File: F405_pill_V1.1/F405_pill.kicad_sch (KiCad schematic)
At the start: 50 parts, among them J1 Conn_01x04_Male, J2 Conn_01x04_Male, J4 TYPE-C-31-M-12, U1 STM32F405RGTx, U2 MAX3051EKA+T, U3 LM1117-3.3, U4 STM32F405_pill, U5 HT7550-1, Y1 Crystal_GND24

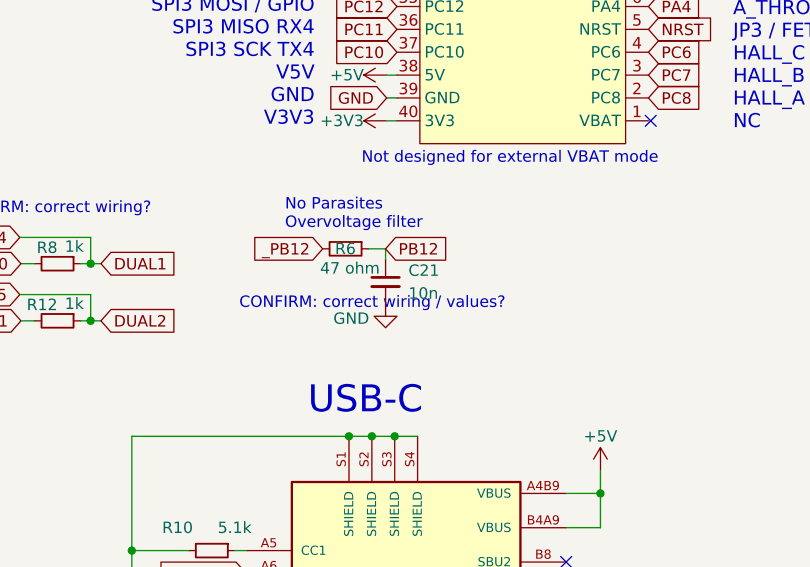
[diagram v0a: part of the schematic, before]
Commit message: changed some part numbers to jlcpcb basic parts
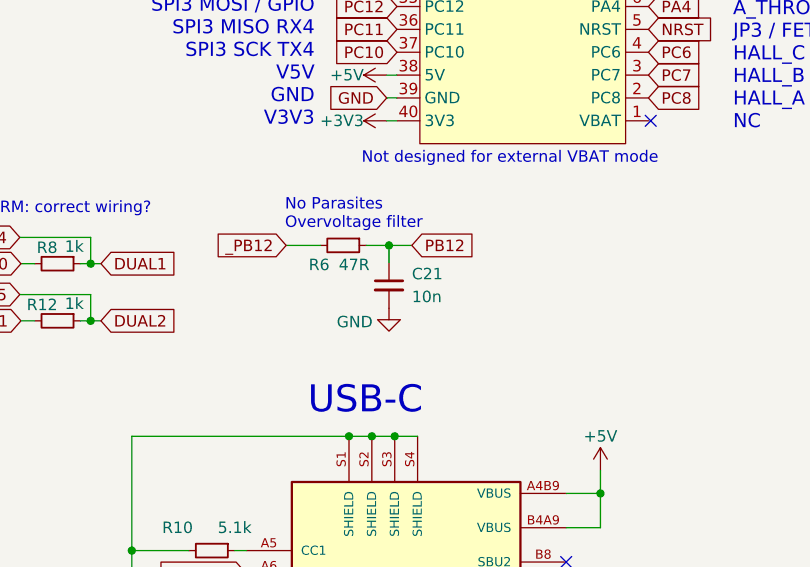
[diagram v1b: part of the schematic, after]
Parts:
- C14, C15: LCSC C41851 -> C1546
- C21, C8: LCSC C527024 -> C15195
- R12, R8: LCSC C25543 -> C11702
- R6: value 47 ohm -> 47R
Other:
- note removed: "CONFIRM: correct wiring / values?"
- moved on the sheet: C21
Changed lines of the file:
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@@
   (junction (at 88.265 115.062) (diameter 0) (color 0 0 0 0)
   )
+  (junction (at 170.815 93.98) (diameter 0) (color 0 0 0 0)
+  )
   (junction (at 69.215 162.052) (diameter 0) (color 0 0 0 0)
   )
@@
     (stroke (width 0) (type default) (color 0 0 0 0))
   )
+  (wire (pts (xy 159.385 93.98) (xy 163.195 93.98))
+    (stroke (width 0) (type default) (color 0 0 0 0))
+  )
   (wire (pts (xy 225.044 135.89) (xy 225.044 134.62))
     (stroke (width 0) (type default) (color 0 0 0 0))
@@
     (stroke (width 0) (type default) (color 0 0 0 0))
   )
+  (wire (pts (xy 170.815 93.98) (xy 168.275 93.98))
+    (stroke (width 0) (type default) (color 0 0 0 0))
+  )
   (wire (pts (xy 146.431 165.862) (xy 144.272 165.862))
     (stroke (width 0) (type default) (color 0 0 0 0))
@@
     (stroke (width 0) (type default) (color 0 0 0 0))
   )
+  (wire (pts (xy 170.815 93.98) (xy 170.815 95.885))
+    (stroke (width 0) (type default) (color 0 0 0 0))
+  )
   (wire (pts (xy 28.702 103.759) (xy 28.702 105.664))
     (stroke (width 0) (type default) (color 0 0 0 0))
@@
     (stroke (width 0) (type default) (color 0 0 0 0))
   )
-  (wire (pts (xy 170.434 95.504) (xy 170.434 94.361))
-    (stroke (width 0) (type default) (color 0 0 0 0))
-  )
   (wire (pts (xy 146.431 171.831) (xy 146.431 173.482))
     (stroke (width 0) (type default) (color 0 0 0 0))
@@
     (stroke (width 0) (type default) (color 0 0 0 0))
   )
-  (wire (pts (xy 170.434 94.361) (xy 168.529 94.361))
+  (wire (pts (xy 173.355 93.98) (xy 170.815 93.98))
     (stroke (width 0) (type default) (color 0 0 0 0))
   )
@@
     (effects (font (size 1.27 1.27)) (justify left bottom))
   )
-  (text "CONFIRM: correct wiring / values?" (at 154.178 101.219 0)
-    (effects (font (size 1.27 1.27)) (justify left bottom))
-  )
   (text "Changes: \nXtal caps from 18pF to 12pF\nSeparate the two LEDs from the single resistor\nNew CAN, with spike protection\nRC between GND and pb12 to stop false trips\nPC12->PA15 to drive LED\nIncreased functionality of several header pins\n"
     (at 155.067 170.688 0)
@@
     )
   )
-  (global_label "_PB12" (shape input) (at 163.449 94.361 180) (fields_autoplaced)
+  (global_label "_PB12" (shape input) (at 159.385 93.98 180) (fields_autoplaced)
     (effects (font (size 1.27 1.27)) (justify right))
-    (property "Intersheet References" "${INTERSHEET_REFS}" (id 0) (at 155.1092 94.2816 0)
+    (property "Intersheet References" "${INTERSHEET_REFS}" (id 0) (at 151.0452 93.9006 0)
       (effects (font (size 1.27 1.27)) (justify right) hide)
     )
@@
     )
   )
-  (global_label "PB12" (shape input) (at 170.434 94.361 0) (fields_autoplaced)
+  (global_label "PB12" (shape input) (at 173.355 93.98 0) (fields_autoplaced)
     (effects (font (size 1.27 1.27)) (justify left))
-    (property "Intersheet References" "${INTERSHEET_REFS}" (id 0) (at 177.8061 94.2816 0)
+    (property "Intersheet References" "${INTERSHEET_REFS}" (id 0) (at 180.7271 93.9006 0)
       (effects (font (size 1.27 1.27)) (justify left) hide)
     )
@@
       (effects (font (size 1.27 1.27)) hide)
     )
-    (property "LCSC" "C25543" (id 4) (at 133.985 102.362 0)
+    (property "LCSC" "C11702" (id 4) (at 133.985 102.362 0)
       (effects (font (size 1.27 1.27)) hide)
     )
@@
       (effects (font (size 1.27 1.27)) hide)
     )
-    (property "LCSC" "C41851" (id 6) (at 79.375 179.832 0)
+    (property "LCSC" "C1546" (id 6) (at 79.375 179.832 0)
       (effects (font (size 1.27 1.27)) hide)
     )
@@
     (pin "1")
   )
-  (symbol (lib_id "Device:R_Small") (at 165.989 94.361 270) (unit 1)
+  (symbol (lib_id "Device:R_Small") (at 165.735 93.98 270) (unit 1)
     (in_bom yes) (on_board yes)
-    (property "Reference" "R6" (id 0) (at 167.132 94.361 90)
+    (property "Reference" "R6" (id 0) (at 164.211 96.139 90)
       (effects (font (size 1.27 1.27)) (justify right))
     )
-    (property "Value" "47 ohm " (id 1) (at 169.799 96.52 90)
+    (property "Value" "47R" (id 1) (at 168.656 96.139 90)
       (effects (font (size 1.27 1.27)) (justify right))
     )
-    (property "Footprint" "Resistor_SMD:R_0402_1005Metric" (id 2) (at 165.989 94.361 0)
+    (property "Footprint" "Resistor_SMD:R_0402_1005Metric" (id 2) (at 165.735 93.98 0)
       (effects (font (size 1.27 1.27)) hide)
     )
-    (property "Datasheet" "~" (id 3) (at 165.989 94.361 0)
+    (property "Datasheet" "~" (id 3) (at 165.735 93.98 0)
       (effects (font (size 1.27 1.27)) hide)
     )
-    (property "LCSC" "C25118" (id 4) (at 165.989 94.361 0)
+    (property "LCSC" "C25118" (id 4) (at 165.735 93.98 0)
       (effects (font (size 1.27 1.27)) hide)
     )
@@
       (effects (font (size 1.27 1.27)) hide)
     )
-    (property "LCSC" "C25543" (id 4) (at 133.985 96.012 0)
+    (property "LCSC" "C11702" (id 4) (at 133.985 96.012 0)
       (effects (font (size 1.27 1.27)) hide)
     )
@@
     (pin "2")
   )
-  (symbol (lib_id "Device:C_Small") (at 170.434 98.044 0) (unit 1)
+  (symbol (lib_id "Device:C_Small") (at 170.815 98.425 0) (unit 1)
     (in_bom yes) (on_board yes)
-    (property "Reference" "C21" (id 0) (at 172.974 96.774 0)
+    (property "Reference" "C21" (id 0) (at 173.355 97.155 0)
       (effects (font (size 1.27 1.27)) (justify left))
     )
-    (property "Value" "10n" (id 1) (at 172.974 99.314 0)
+    (property "Value" "10n" (id 1) (at 173.355 99.695 0)
       (effects (font (size 1.27 1.27)) (justify left))
     )
-    (property "Footprint" "Capacitor_SMD:C_0402_1005Metric" (id 2) (at 170.434 98.044 0)
+    (property "Footprint" "Capacitor_SMD:C_0402_1005Metric" (id 2) (at 170.815 98.425 0)
       (effects (font (size 1.27 1.27)) hide)
     )
-    (property "Datasheet" "~" (id 3) (at 170.434 98.044 0)
+    (property "Datasheet" "~" (id 3) (at 170.815 98.425 0)
       (effects (font (size 1.27 1.27)) hide)
     )
-    (property "LCSC" "C527024" (id 6) (at 170.434 98.044 0)
+    (property "LCSC" "C15195" (id 6) (at 170.815 98.425 0)
       (effects (font (size 1.27 1.27)) hide)
     )
@@
       (effects (font (size 1.27 1.27)) hide)
     )
-    (property "LCSC" "C41851" (id 6) (at 76.835 165.862 0)
+    (property "LCSC" "C1546" (id 6) (at 76.835 165.862 0)
       (effects (font (size 1.27 1.27)) hide)
     )
@@
       (effects (font (size 1.27 1.27)) hide)
     )
-    (property "LCSC" "C527024" (id 6) (at 47.117 144.526 0)
+    (property "LCSC" "C15195" (id 6) (at 47.117 144.526 0)
       (effects (font (size 1.27 1.27)) hide)
     )
@@
     (pin "4")
   )
-  (symbol (lib_id "power:GND") (at 170.434 100.584 0) (unit 1)
+  (symbol (lib_id "power:GND") (at 170.815 100.965 0) (unit 1)
     (in_bom yes) (on_board yes)
-    (property "Reference" "#PWR0101" (id 0) (at 170.434 106.934 0)
+    (property "Reference" "#PWR0101" (id 0) (at 170.815 107.315 0)
       (effects (font (size 1.27 1.27)) hide)
     )
-    (property "Value" "GND" (id 1) (at 166.624 102.108 0))
-    (property "Footprint" "" (id 2) (at 170.434 100.584 0)
+    (property "Value" "GND" (id 1) (at 167.005 102.489 0))
+    (property "Footprint" "" (id 2) (at 170.815 100.965 0)
       (effects (font (size 1.27 1.27)) hide)
     )
-    (property "Datasheet" "" (id 3) (at 170.434 100.584 0)
+    (property "Datasheet" "" (id 3) (at 170.815 100.965 0)
       (effects (font (size 1.27 1.27)) hide)
     )
@@
     )
     (path "/6a4f5718-b00e-497b-8cfa-66648221e102"
-      (reference "R6") (unit 1) (value "47 ohm ") (footprint "Resistor_SMD:R_0402_1005Metric")
+      (reference "R6") (unit 1) (value "47R") (footprint "Resistor_SMD:R_0402_1005Metric")
     )
     (path "/6d03381c-2f3a-4ea6-9173-4951d09886cc"

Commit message: fixed some LC parts
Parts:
- C3, C6: LCSC C1642 -> C1547
- D1: footprint LED_SMD:LED_0402_1005Metric_Pad0.77x0.64mm_HandSolder -> LED_SMD:LED_0603_1608Metric; LCSC C130724 -> C72041
- D2: footprint LED_SMD:LED_0402_1005Metric_Pad0.77x0.64mm_HandSolder -> LED_SMD:LED_0603_1608Metric; LCSC C130719 -> C72043
- D3: footprint LED_SMD:LED_0402_1005Metric_Pad0.77x0.64mm_HandSolder -> LED_SMD:LED_0603_1608Metric; LCSC C434445 -> C2286
- R1, R2: LCSC C140214 -> C25086
- R3, R4: footprint Resistor_SMD:R_0402_1005Metric -> Resistor_SMD:R_0603_1608Metric; LCSC C60310 -> C4216
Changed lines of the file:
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@@
       (effects (font (size 1.27 1.27)) hide)
     )
-    (property "LCSC" "C140214" (id 6) (at 40.005 38.989 0)
+    (property "LCSC" "C25086" (id 6) (at 40.005 38.989 0)
       (effects (font (size 1.27 1.27)) hide)
     )
@@
       (effects (font (size 1.27 1.27)) hide)
     )
-    (property "LCSC" "C1642" (id 4) (at 46.355 66.929 0)
+    (property "LCSC" "C1547" (id 4) (at 46.355 66.929 0)
       (effects (font (size 1.27 1.27)) hide)
     )
@@
       (effects (font (size 1.27 1.27)) hide)
     )
-    (property "LCSC" "C1642" (id 4) (at 31.75 66.929 0)
+    (property "LCSC" "C1547" (id 4) (at 31.75 66.929 0)
       (effects (font (size 1.27 1.27)) hide)
     )
@@
       (effects (font (size 1.27 1.27)) (justify right) hide)
     )
-    (property "Footprint" "Resistor_SMD:R_0402_1005Metric" (id 2) (at 69.215 173.482 0)
+    (property "Footprint" "Resistor_SMD:R_0603_1608Metric" (id 2) (at 69.215 173.482 0)
       (effects (font (size 1.27 1.27)) hide)
     )
@@
       (effects (font (size 1.27 1.27)) hide)
     )
-    (property "LCSC" "C60310" (id 6) (at 69.215 173.482 0)
+    (property "LCSC" "C4216" (id 6) (at 69.215 173.482 0)
       (effects (font (size 1.27 1.27)) hide)
     )
@@
       (effects (font (size 1.27 1.27)) (justify right) hide)
     )
-    (property "Footprint" "Resistor_SMD:R_0402_1005Metric" (id 2) (at 69.215 165.862 0)
+    (property "Footprint" "Resistor_SMD:R_0603_1608Metric" (id 2) (at 69.215 165.862 0)
       (effects (font (size 1.27 1.27)) hide)
     )
@@
       (effects (font (size 1.27 1.27)) hide)
     )
-    (property "LCSC" "C60310" (id 6) (at 69.215 165.862 0)
+    (property "LCSC" "C4216" (id 6) (at 69.215 165.862 0)
       (effects (font (size 1.27 1.27)) hide)
     )
@@
     )
     (property "Value" "BLU" (id 1) (at 25.146 99.822 0))
-    (property "Footprint" "LED_SMD:LED_0402_1005Metric_Pad0.77x0.64mm_HandSolder" (id 2) (at 23.241 101.219 90)
+    (property "Footprint" "LED_SMD:LED_0603_1608Metric" (id 2) (at 23.241 101.219 90)
       (effects (font (size 1.27 1.27)) hide)
     )
@@
       (effects (font (size 1.27 1.27)) hide)
     )
-    (property "LCSC" "C130724" (id 6) (at 23.241 101.219 0)
+    (property "LCSC" "C72041" (id 6) (at 23.241 101.219 0)
       (effects (font (size 1.27 1.27)) hide)
     )
@@
     )
     (property "Value" "RED" (id 1) (at 37.338 100.203 0))
-    (property "Footprint" "LED_SMD:LED_0402_1005Metric_Pad0.77x0.64mm_HandSolder" (id 2) (at 35.052 101.346 90)
+    (property "Footprint" "LED_SMD:LED_0603_1608Metric" (id 2) (at 35.052 101.346 90)
       (effects (font (size 1.27 1.27)) hide)
     )
@@
       (effects (font (size 1.27 1.27)) hide)
     )
-    (property "LCSC" "C434445" (id 6) (at 35.052 101.346 0)
+    (property "LCSC" "C2286" (id 6) (at 35.052 101.346 0)
       (effects (font (size 1.27 1.27)) hide)
     )
@@
       (effects (font (size 1.27 1.27)) hide)
     )
-    (property "LCSC" "C140214" (id 6) (at 59.055 22.479 0)
+    (property "LCSC" "C25086" (id 6) (at 59.055 22.479 0)
       (effects (font (size 1.27 1.27)) hide)
     )
@@
     )
     (property "Value" "GRN" (id 1) (at 30.734 100.076 0))
-    (property "Footprint" "LED_SMD:LED_0402_1005Metric_Pad0.77x0.64mm_HandSolder" (id 2) (at 28.702 101.219 90)
+    (property "Footprint" "LED_SMD:LED_0603_1608Metric" (id 2) (at 28.702 101.219 90)
       (effects (font (size 1.27 1.27)) hide)
     )
@@
       (effects (font (size 1.27 1.27)) hide)
     )
-    (property "LCSC" "C130719" (id 6) (at 28.702 101.219 0)
+    (property "LCSC" "C72043" (id 6) (at 28.702 101.219 0)
       (effects (font (size 1.27 1.27)) hide)
     )
@@
     )
     (path "/ea699d5d-18e1-4b3b-b25a-971d32e2e1c2"
-      (reference "D1") (unit 1) (value "BLU") (footprint "LED_SMD:LED_0402_1005Metric_Pad0.77x0.64mm_HandSolder")
+      (reference "D1") (unit 1) (value "BLU") (footprint "LED_SMD:LED_0603_1608Metric")
     )
     (path "/fba4c573-34bb-4e81-a728-e13c229abcc7"
-      (reference "D2") (unit 1) (value "GRN") (footprint "LED_SMD:LED_0402_1005Metric_Pad0.77x0.64mm_HandSolder")
+      (reference "D2") (unit 1) (value "GRN") (footprint "LED_SMD:LED_0603_1608Metric")
     )
     (path "/f8fc2924-31bc-41cd-8ee8-525d186d8824"
-      (reference "D3") (unit 1) (value "RED") (footprint "LED_SMD:LED_0402_1005Metric_Pad0.77x0.64mm_HandSolder")
+      (reference "D3") (unit 1) (value "RED") (footprint "LED_SMD:LED_0603_1608Metric")
     )
     (path "/ae565f66-d769-4a64-a812-22d0aabaeb28"
@@
     )
     (path "/c94eb5d4-d4fd-4174-84ff-5b04692ded2b"
-      (reference "R3") (unit 1) (value "60 ohm") (footprint "Resistor_SMD:R_0402_1005Metric")
+      (reference "R3") (unit 1) (value "60 ohm") (footprint "Resistor_SMD:R_0603_1608Metric")
     )
     (path "/86ccb56e-66bb-47e4-9bb8-736d070a8f03"
-      (reference "R4") (unit 1) (value "60 ohm") (footprint "Resistor_SMD:R_0402_1005Metric")
+      (reference "R4") (unit 1) (value "60 ohm") (footprint "Resistor_SMD:R_0603_1608Metric")
     )
     (path "/88bfc4e5-d56b-4c8b-b460-b5c6db60e044"
